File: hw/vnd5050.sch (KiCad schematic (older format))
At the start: 9 parts, among them U401 VND5050AJTR-E

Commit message: 1.0 pcb created
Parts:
- removed C703: 4.7uF, kemet:0603, symbol 4.7uF
- removed R402: 390, yageo:0603, symbol 390
- added D301: DIODE_RS07J-GS18, usevolt:DO219AB, symbol usevolt:DIODE_RS07J-GS18
- C301: renamed from C702; symbol 4.7uF -> kemet:4.7uF
- D302: renamed from D701; symbol DIODE_RS07J-GS18 -> usevolt:DIODE_RS07J-GS18
- D303: renamed from D702; symbol DIODE_RS07J-GS18 -> usevolt:DIODE_RS07J-GS18
- R301: renamed from R403; symbol 1K -> yageo:1K
- R302: renamed from R404; symbol 1K -> yageo:1K
- R303: renamed from R401; symbol 390 -> yageo:390
- U301: renamed from U401; symbol VND5050AJTR-E -> usevolt:VND5050AJTR-E
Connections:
- net labels added: +3V3, SENSE
- net labels removed: SENSE1, SENSE2
- wire segments 37 -> 48

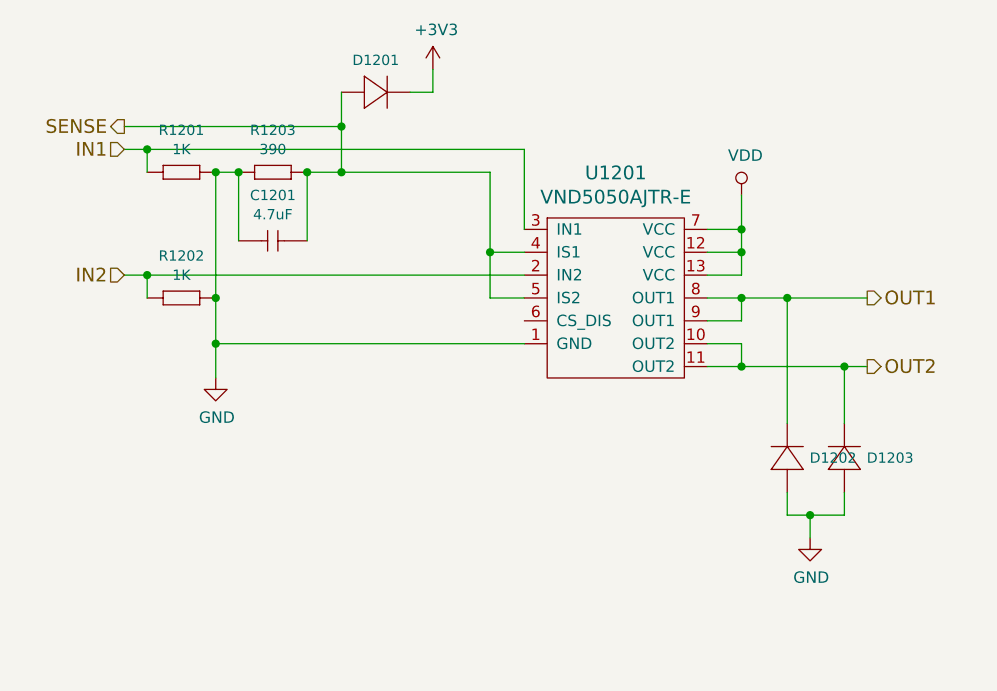
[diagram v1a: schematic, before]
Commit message: pull down resistor and flyback diode added to out11
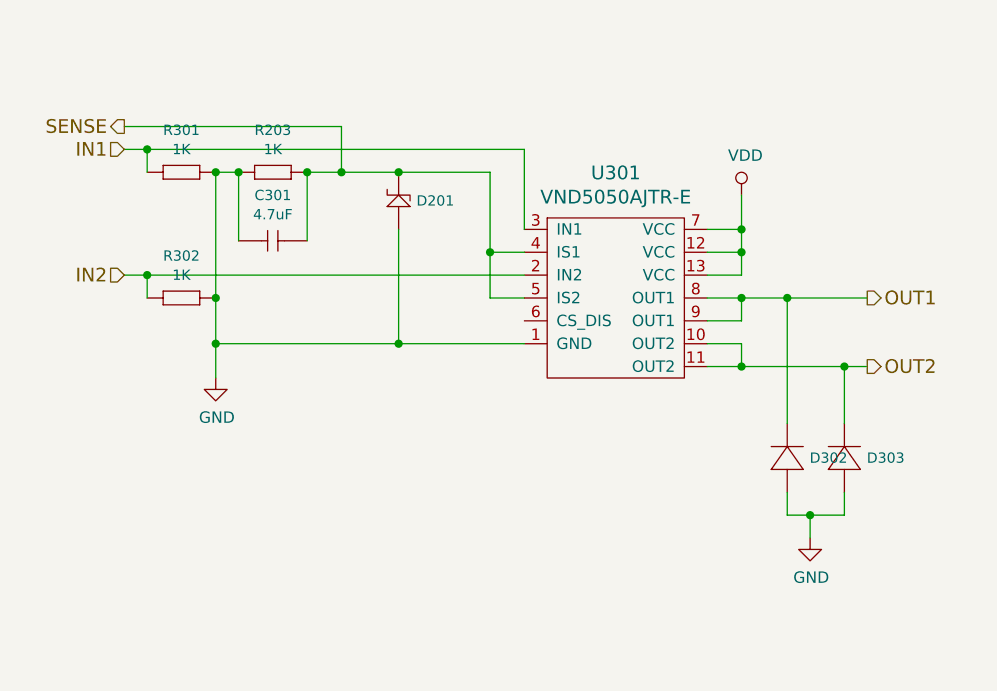
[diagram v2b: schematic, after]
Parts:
- removed D301: DIODE_RS07J-GS18, usevolt:DO219AB, symbol usevolt:DIODE_RS07J-GS18
- removed R303: 390, yageo:0603, symbol yageo:390
- added D901: ZENER_MM3Z3V6T1G, usevolt:SOD-323, symbol usevolt:ZENER_MM3Z3V6T1G
- added R203: 1K, yageo:0603, symbol yageo:1K
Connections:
- net GND: now also D901.2, R203.2 (R2)
- net SENSE: now also D901.1, R203.1 (R1)
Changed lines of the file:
@@
 $Descr A4 11693 8268
 encoding utf-8
-Sheet 5 15
+Sheet 9 15
 Title ""
 Date ""
@@
 AR Path="/5A8DEA06/59D8088A" Ref="U1101"  Part="1"
 AR Path="/5A8DF701/59D8088A" Ref="U1201"  Part="1"
-F 0 "U1201" H 4700 4447 60  0000 C CNN
+F 0 "U301" H 4700 4447 60  0000 C CNN
 F 1 "VND5050AJTR-E" H 4700 4341 60  0000 C CNN
 F 2 "usevolt:PowerSSO-12" H 4600 4400 60  0001 C CNN
@@
 AR Path="/5A8DEA06/59D808C7" Ref="#PWR01103"  Part="1"
 AR Path="/5A8DF701/59D808C7" Ref="#PWR01203"  Part="1"
-F 0 "#PWR01203" H 5250 3500 50  0001 C CNN
+F 0 "#PWR0303" H 5250 3500 50  0001 C CNN
 F 1 "VDD" H 5267 3823 50  0000 C CNN
 F 2 "" H 5250 3650 50  0000 C CNN
@@
 AR Path="/5A8DEA06/59D86DC2" Ref="#PWR01101"  Part="1"
 AR Path="/5A8DF701/59D86DC2" Ref="#PWR01201"  Part="1"
-F 0 "#PWR01201" H 2950 4200 50  0001 C CNN
+F 0 "#PWR0301" H 2950 4200 50  0001 C CNN
 F 1 "GND" H 2955 4277 50  0000 C CNN
 F 2 "" H 2950 4450 50  0000 C CNN
 F 3 "" H 2950 4450 50  0000 C CNN
 	1    2950 4450
-	1    0    0    -1
-$EndComp
-$Comp
-L yageo:390 R?
-U 1 1 59D88845
-P 3150 3550
-AR Path="/5A015FC0/59D88845" Ref="R?"  Part="1"
-AR Path="/5A02A41F/59D88845" Ref="R?"  Part="1"
-AR Path="/5A12B58E/59D88845" Ref="R?"  Part="1"
-AR Path="/5A7B157A/59D88845" Ref="R?"  Part="1"
-AR Path="/5A7B341B/59D88845" Ref="R?"  Part="1"
-AR Path="/5A7B2C1B/59D88845" Ref="R?"  Part="1"
-AR Path="/5A7B3FAD/59D88845" Ref="R?"  Part="1"
-AR Path="/5A7B4C13/59D88845" Ref="R?"  Part="1"
-AR Path="/5A7B577E/59D88845" Ref="R?"  Part="1"
-AR Path="/5A7B753D/59D88845" Ref="R?"  Part="1"
-AR Path="/5A8D7860/59D88845" Ref="R303"  Part="1"
-AR Path="/5A8D8BD2/59D88845" Ref="R403"  Part="1"
-AR Path="/5A8D900F/59D88845" Ref="R503"  Part="1"
-AR Path="/5A8D95F3/59D88845" Ref="R603"  Part="1"
-AR Path="/5A8D9C64/59D88845" Ref="R703"  Part="1"
-AR Path="/5A8DA46E/59D88845" Ref="R803"  Part="1"
-AR Path="/5A8DB2AD/59D88845" Ref="R903"  Part="1"
-AR Path="/5A8DBBEF/59D88845" Ref="R1003"  Part="1"
-AR Path="/5A8DEA06/59D88845" Ref="R1103"  Part="1"
-AR Path="/5A8DF701/59D88845" Ref="R1203"  Part="1"
-F 0 "R1203" H 3200 3734 45  0000 C CNN
-F 1 "390" H 3200 3650 45  0000 C CNN
-F 2 "yageo:0603" H 3180 3700 20  0001 C CNN
-F 3 "" H 3119 3589 60  0001 C CNN
-F 4 "" H 3519 3989 60  0001 C CNN "1st Source Part Number"
-F 5 "Digikey" H 3419 3889 60  0001 C CNN "1st Source"
-F 6 "RC0603FR-07390RL" H 3319 3789 60  0001 C CNN "Manufacturer Part Number"
-F 7 "YAGEO" H 3219 3689 60  0001 C CNN "Manufacturer"
-	1    3150 3550
 	1    0    0    -1
 $EndComp
@@
 AR Path="/5A8DEA06/5A05950C" Ref="R1101"  Part="1"
 AR Path="/5A8DF701/5A05950C" Ref="R1201"  Part="1"
-F 0 "R1201" H 2800 3734 45  0000 C CNN
+F 0 "R301" H 2800 3734 45  0000 C CNN
 F 1 "1K" H 2800 3650 45  0000 C CNN
 F 2 "yageo:0603" H 2780 3700 20  0001 C CNN
@@
 AR Path="/5A8DEA06/5A059568" Ref="R1102"  Part="1"
 AR Path="/5A8DF701/5A059568" Ref="R1202"  Part="1"
-F 0 "R1202" H 2800 4284 45  0000 C CNN
+F 0 "R302" H 2800 4284 45  0000 C CNN
 F 1 "1K" H 2800 4200 45  0000 C CNN
 F 2 "yageo:0603" H 2780 4250 20  0001 C CNN
@@
 AR Path="/5A8DEA06/5A2AAF9E" Ref="D1102"  Part="1"
 AR Path="/5A8DF701/5A2AAF9E" Ref="D1202"  Part="1"
-F 0 "D1202" V 5400 4652 45  0000 R CNN
+F 0 "D302" V 5400 4652 45  0000 R CNN
 F 1 "DIODE_RS07J-GS18" H 5470 4690 45  0001 L BNN
 F 2 "usevolt:DO219AB" H 5480 4900 20  0001 C CNN
@@
 AR Path="/5A8DEA06/5A2AB087" Ref="D1103"  Part="1"
 AR Path="/5A8DF701/5A2AB087" Ref="D1203"  Part="1"
-F 0 "D1203" V 5650 4652 45  0000 R CNN
+F 0 "D303" V 5650 4652 45  0000 R CNN
 F 1 "DIODE_RS07J-GS18" H 5720 4690 45  0001 L BNN
 F 2 "usevolt:DO219AB" H 5730 4900 20  0001 C CNN
@@
 AR Path="/5A8DEA06/5A2AB10F" Ref="#PWR01104"  Part="1"
 AR Path="/5A8DF701/5A2AB10F" Ref="#PWR01204"  Part="1"
-F 0 "#PWR01204" H 5550 4900 50  0001 C CNN
+F 0 "#PWR0304" H 5550 4900 50  0001 C CNN
 F 1 "GND" H 5555 4977 50  0000 C CNN
 F 2 "" H 5550 5150 50  0000 C CNN
@@
 	2950 3550 2950 4100
 Wire Wire Line
-	2950 4300 4300 4300
+	2950 4300 3750 4300
 Wire Wire Line
 	3050 3550 2950 3550
@@
 Wire Wire Line
 	3350 3550 3500 3550
-Wire Wire Line
-	3500 3200 3500 3350
 Wire Wire Line
 	3500 3350 2550 3350
@@
 AR Path="/5A8DEA06/5A708309" Ref="C1101"  Part="1"
 AR Path="/5A8DF701/5A708309" Ref="C1201"  Part="1"
-F 0 "C1201" H 3200 4049 45  0000 C CNN
+F 0 "C301" H 3200 4049 45  0000 C CNN
 F 1 "4.7uF" H 3200 3965 45  0000 C CNN
 F 2 "kemet:0603" H 3180 4000 20  0001 C CNN
@@
 Wire Wire Line
 	3050 3850 3050 3550
-Connection ~ 3050 3550
 Wire Wire Line
 	3350 3850 3350 3550
-Connection ~ 3350 3550
 Wire Wire Line
 	4150 4100 4300 4100
 Connection ~ 4150 3900
-$Comp
-L usevolt:DIODE_RS07J-GS18 D?
-U 1 1 5A7BC689
-P 3700 3200
-AR Path="/5A7B157A/5A7BC689" Ref="D?"  Part="1"
-AR Path="/5A7B341B/5A7BC689" Ref="D?"  Part="1"
-AR Path="/5A7B2C1B/5A7BC689" Ref="D?"  Part="1"
-AR Path="/5A7B3FAD/5A7BC689" Ref="D?"  Part="1"
-AR Path="/5A7B4C13/5A7BC689" Ref="D?"  Part="1"
-AR Path="/5A7B577E/5A7BC689" Ref="D?"  Part="1"
-AR Path="/5A7B753D/5A7BC689" Ref="D?"  Part="1"
-AR Path="/5A8D7860/5A7BC689" Ref="D301"  Part="1"
-AR Path="/5A8D8BD2/5A7BC689" Ref="D401"  Part="1"
-AR Path="/5A8D900F/5A7BC689" Ref="D501"  Part="1"
-AR Path="/5A8D95F3/5A7BC689" Ref="D601"  Part="1"
-AR Path="/5A8D9C64/5A7BC689" Ref="D701"  Part="1"
-AR Path="/5A8DA46E/5A7BC689" Ref="D801"  Part="1"
-AR Path="/5A8DB2AD/5A7BC689" Ref="D901"  Part="1"
-AR Path="/5A8DBBEF/5A7BC689" Ref="D1001"  Part="1"
-AR Path="/5A8DEA06/5A7BC689" Ref="D1101"  Part="1"
-AR Path="/5A8DF701/5A7BC689" Ref="D1201"  Part="1"
-F 0 "D1201" H 3650 3340 45  0000 C CNN
-F 1 "DIODE_RS07J-GS18" H 3720 3140 45  0001 L BNN
-F 2 "usevolt:DO219AB" H 3730 3350 20  0001 C CNN
-F 3 "http://www.vishay.com/docs/85742/rs07b.pdf" H 3720 3220 60  0001 C CNN
-F 4 "1864882" H 4320 3820 60  0001 C CNN "2nd Source Part Number"
-F 5 "Digi-Key" H 4020 3520 60  0001 C CNN "1st Source"
-F 6 "Farnell" H 4220 3720 60  0001 C CNN "2nd Source"
-F 7 "RS07J-GS18" H 3920 3420 60  0001 C CNN "Manufacturer Part Number"
-F 8 "RS07J-GS18-ND" H 4120 3620 60  0001 C CNN "1st Source Part Number"
-F 9 "Vishay Semiconductor Diodes Division" H 3820 3320 60  0001 C CNN "Manufacturer"
-	1    3700 3200
-	1    0    0    -1
-$EndComp
-Connection ~ 3500 3350
-$Comp
-L power:+3V3 #PWR0302
-U 1 1 5A7BC750
-P 3900 3100
-AR Path="/5A8D7860/5A7BC750" Ref="#PWR0302"  Part="1"
-AR Path="/5A8D8BD2/5A7BC750" Ref="#PWR0402"  Part="1"
-AR Path="/5A8D900F/5A7BC750" Ref="#PWR0502"  Part="1"
-AR Path="/5A8D95F3/5A7BC750" Ref="#PWR0602"  Part="1"
-AR Path="/5A8D9C64/5A7BC750" Ref="#PWR0702"  Part="1"
-AR Path="/5A8DA46E/5A7BC750" Ref="#PWR0802"  Part="1"
-AR Path="/5A8DB2AD/5A7BC750" Ref="#PWR0902"  Part="1"
-AR Path="/5A8DBBEF/5A7BC750" Ref="#PWR01002"  Part="1"
-AR Path="/5A8DEA06/5A7BC750" Ref="#PWR01102"  Part="1"
-AR Path="/5A8DF701/5A7BC750" Ref="#PWR01202"  Part="1"
-F 0 "#PWR01202" H 3900 2950 50  0001 C CNN
-F 1 "+3V3" H 3915 3273 50  0000 C CNN
-F 2 "" H 3900 3100 50  0000 C CNN
-F 3 "" H 3900 3100 50  0000 C CNN
-	1    3900 3100
-	1    0    0    -1
-$EndComp
-Wire Wire Line
-	3900 3100 3900 3200
-Wire Wire Line
-	3900 3200 3800 3200
 Wire Wire Line
 	5250 3800 5250 3900
@@
 	2950 4100 2950 4300
 Wire Wire Line
-	3500 3550 4150 3550
+	3500 3550 3750 3550
 Wire Wire Line
 	2650 3450 4300 3450
@@
 Wire Wire Line
 	3500 3350 3500 3550
+$Comp
+L yageo:1K R203
+U 1 1 5B6F848F
+P 3150 3550
+AR Path="/5A8D7860/5B6F848F" Ref="R203"  Part="1"
+AR Path="/5A8D8BD2/5B6F848F" Ref="R303"  Part="1"
+AR Path="/5A8D900F/5B6F848F" Ref="R403"  Part="1"
+AR Path="/5A8D95F3/5B6F848F" Ref="R503"  Part="1"
+AR Path="/5A8D9C64/5B6F848F" Ref="R603"  Part="1"
+AR Path="/5A8DA46E/5B6F848F" Ref="R703"  Part="1"
+AR Path="/5A8DB2AD/5B6F848F" Ref="R803"  Part="1"
+AR Path="/5A8DBBEF/5B6F848F" Ref="R903"  Part="1"
+AR Path="/5A8DEA06/5B6F848F" Ref="R1003"  Part="1"
+AR Path="/5A8DF701/5B6F848F" Ref="R1103"  Part="1"
+F 0 "R203" H 3200 3734 45  0000 C CNN
+F 1 "1K" H 3200 3650 45  0000 C CNN
+F 2 "yageo:0603" H 3180 3700 20  0001 C CNN
+F 3 "" H 3119 3589 60  0001 C CNN
+F 4 "" H 3519 3989 60  0001 C CNN "1st Source Part Number"
+F 5 "Digikey" H 3419 3889 60  0001 C CNN "1st Source"
+F 6 "RC0603FR-071KL" H 3319 3789 60  0001 C CNN "Manufacturer Part Number"
+F 7 "YAGEO" H 3219 3689 60  0001 C CNN "Manufacturer"
+	1    3150 3550
+	1    0    0    -1
+$EndComp
+Connection ~ 3350 3550
+Connection ~ 3050 3550
+$Comp
+L usevolt:ZENER_MM3Z3V6T1G D901
+U 1 1 5B701DAD
+P 3750 3600
+AR Path="/5A8DBBEF/5B701DAD" Ref="D901"  Part="1"
+AR Path="/5A8D7860/5B701DAD" Ref="D201"  Part="1"
+AR Path="/5A8D8BD2/5B701DAD" Ref="D301"  Part="1"
+AR Path="/5A8D900F/5B701DAD" Ref="D401"  Part="1"
+AR Path="/5A8D95F3/5B701DAD" Ref="D501"  Part="1"
+AR Path="/5A8D9C64/5B701DAD" Ref="D601"  Part="1"
+AR Path="/5A8DA46E/5B701DAD" Ref="D701"  Part="1"
+AR Path="/5A8DB2AD/5B701DAD" Ref="D801"  Part="1"
+AR Path="/5A8DEA06/5B701DAD" Ref="D1001"  Part="1"
+AR Path="/5A8DF701/5B701DAD" Ref="D1101"  Part="1"
+F 0 "D201" V 3675 3522 45  0000 R CNN
+F 1 "ZENER_MM3Z3V6T1G" H 4025 3975 45  0001 L BNN
+F 2 "usevolt:SOD-323" H 3725 3975 20  0001 C CNN
+F 3 "http://www.mouser.com/ds/2/308/MM3Z2V4T1-D-269162.pdf" H 4100 4175 60  0001 C CNN
+F 4 "Mouser" H 4070 3920 60  0001 C CNN "1st Source"
+F 5 "MM3Z3V6T1G" H 3970 3820 60  0001 C CNN "Manufacturer Part Number"
+F 6 "863-MM3Z3V6T1G" H 4170 4020 60  0001 C CNN "1st Source Part Number"
+F 7 "ON Semiconductor" H 4025 4075 60  0001 C CNN "Manufacturer"
+	1    3750 3600
+	0    -1   -1   0
+$EndComp
+Connection ~ 3750 3550
+Wire Wire Line
+	3750 3550 4150 3550
+Wire Wire Line
+	3750 3800 3750 4300
+Connection ~ 3750 4300
+Wire Wire Line
+	3750 4300 4300 4300
 $EndSCHEMATC

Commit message: pcb 1.3.0 created
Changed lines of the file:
@@
 AR Path="/5A8DEA06/59D8088A" Ref="U1101"  Part="1"
 AR Path="/5A8DF701/59D8088A" Ref="U1201"  Part="1"
-F 0 "U301" H 4700 4447 60  0000 C CNN
+F 0 "U1201" H 4700 4447 60  0000 C CNN
 F 1 "VND5050AJTR-E" H 4700 4341 60  0000 C CNN
 F 2 "usevolt:PowerSSO-12" H 4600 4400 60  0001 C CNN
@@
 AR Path="/5A8DEA06/59D808C7" Ref="#PWR01103"  Part="1"
 AR Path="/5A8DF701/59D808C7" Ref="#PWR01203"  Part="1"
-F 0 "#PWR0303" H 5250 3500 50  0001 C CNN
+F 0 "#PWR01203" H 5250 3500 50  0001 C CNN
 F 1 "VDD" H 5267 3823 50  0000 C CNN
 F 2 "" H 5250 3650 50  0000 C CNN
@@
 AR Path="/5A8DEA06/59D86DC2" Ref="#PWR01101"  Part="1"
 AR Path="/5A8DF701/59D86DC2" Ref="#PWR01201"  Part="1"
-F 0 "#PWR0301" H 2950 4200 50  0001 C CNN
+F 0 "#PWR01201" H 2950 4200 50  0001 C CNN
 F 1 "GND" H 2955 4277 50  0000 C CNN
 F 2 "" H 2950 4450 50  0000 C CNN
@@
 AR Path="/5A8DEA06/5A05950C" Ref="R1101"  Part="1"
 AR Path="/5A8DF701/5A05950C" Ref="R1201"  Part="1"
-F 0 "R301" H 2800 3734 45  0000 C CNN
+F 0 "R1201" H 2800 3734 45  0000 C CNN
 F 1 "1K" H 2800 3650 45  0000 C CNN
 F 2 "yageo:0603" H 2780 3700 20  0001 C CNN
@@
 AR Path="/5A8DEA06/5A059568" Ref="R1102"  Part="1"
 AR Path="/5A8DF701/5A059568" Ref="R1202"  Part="1"
-F 0 "R302" H 2800 4284 45  0000 C CNN
+F 0 "R1202" H 2800 4284 45  0000 C CNN
 F 1 "1K" H 2800 4200 45  0000 C CNN
 F 2 "yageo:0603" H 2780 4250 20  0001 C CNN
@@
 AR Path="/5A8DEA06/5A2AAF9E" Ref="D1102"  Part="1"
 AR Path="/5A8DF701/5A2AAF9E" Ref="D1202"  Part="1"
-F 0 "D302" V 5400 4652 45  0000 R CNN
+F 0 "D1202" V 5400 4652 45  0000 R CNN
 F 1 "DIODE_RS07J-GS18" H 5470 4690 45  0001 L BNN
 F 2 "usevolt:DO219AB" H 5480 4900 20  0001 C CNN
@@
 AR Path="/5A8DEA06/5A2AB087" Ref="D1103"  Part="1"
 AR Path="/5A8DF701/5A2AB087" Ref="D1203"  Part="1"
-F 0 "D303" V 5650 4652 45  0000 R CNN
+F 0 "D1203" V 5650 4652 45  0000 R CNN
 F 1 "DIODE_RS07J-GS18" H 5720 4690 45  0001 L BNN
 F 2 "usevolt:DO219AB" H 5730 4900 20  0001 C CNN
@@
 AR Path="/5A8DEA06/5A2AB10F" Ref="#PWR01104"  Part="1"
 AR Path="/5A8DF701/5A2AB10F" Ref="#PWR01204"  Part="1"
-F 0 "#PWR0304" H 5550 4900 50  0001 C CNN
+F 0 "#PWR01204" H 5550 4900 50  0001 C CNN
 F 1 "GND" H 5555 4977 50  0000 C CNN
 F 2 "" H 5550 5150 50  0000 C CNN
@@
 AR Path="/5A8DEA06/5A708309" Ref="C1101"  Part="1"
 AR Path="/5A8DF701/5A708309" Ref="C1201"  Part="1"
-F 0 "C301" H 3200 4049 45  0000 C CNN
+F 0 "C1201" H 3200 4049 45  0000 C CNN
 F 1 "4.7uF" H 3200 3965 45  0000 C CNN
 F 2 "kemet:0603" H 3180 4000 20  0001 C CNN
@@
 AR Path="/5A8DEA06/5B6F848F" Ref="R1003"  Part="1"
 AR Path="/5A8DF701/5B6F848F" Ref="R1103"  Part="1"
-F 0 "R203" H 3200 3734 45  0000 C CNN
+F 0 "R1103" H 3200 3734 45  0000 C CNN
 F 1 "1K" H 3200 3650 45  0000 C CNN
 F 2 "yageo:0603" H 3180 3700 20  0001 C CNN
@@
 AR Path="/5A8DEA06/5B701DAD" Ref="D1001"  Part="1"
 AR Path="/5A8DF701/5B701DAD" Ref="D1101"  Part="1"
-F 0 "D201" V 3675 3522 45  0000 R CNN
+F 0 "D1101" V 3675 3522 45  0000 R CNN
 F 1 "ZENER_MM3Z3V6T1G" H 4025 3975 45  0001 L BNN
 F 2 "usevolt:SOD-323" H 3725 3975 20  0001 C CNN
